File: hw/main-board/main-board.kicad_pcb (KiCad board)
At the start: 2 copper layers, 42 x 42 mm, 61 parts, among them J1 USB_C_Receptacle_USB2.0_16P, J2 S4B-XH-A_LF__SN_, J3 S4B-XH-A_LF__SN_, Q1 AONR21307, U1 HUSB238_xxxDD, U2 AP63205WU, U3 AP2112K-3.3, U4 PTR54L, U5 TMC2226-SA, U6 TMC2226-SA

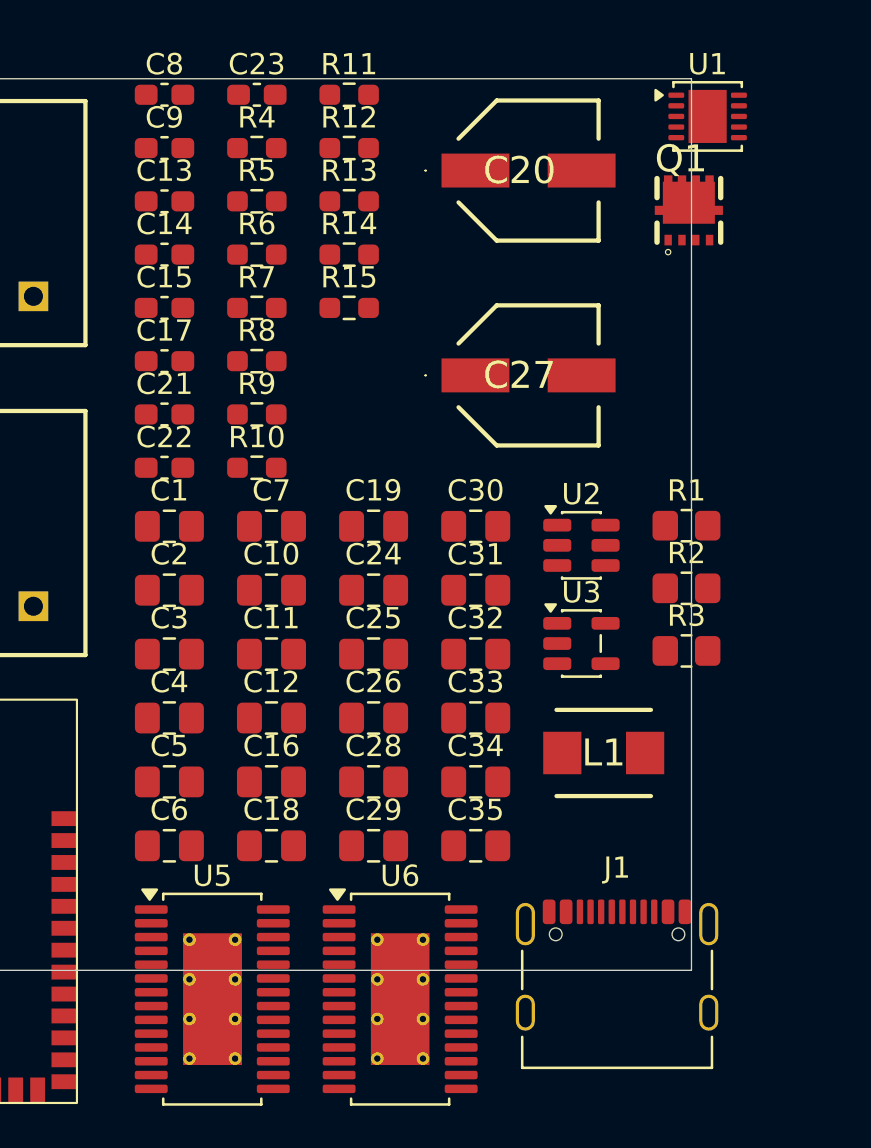
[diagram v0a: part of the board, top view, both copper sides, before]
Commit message: Add indicator LED
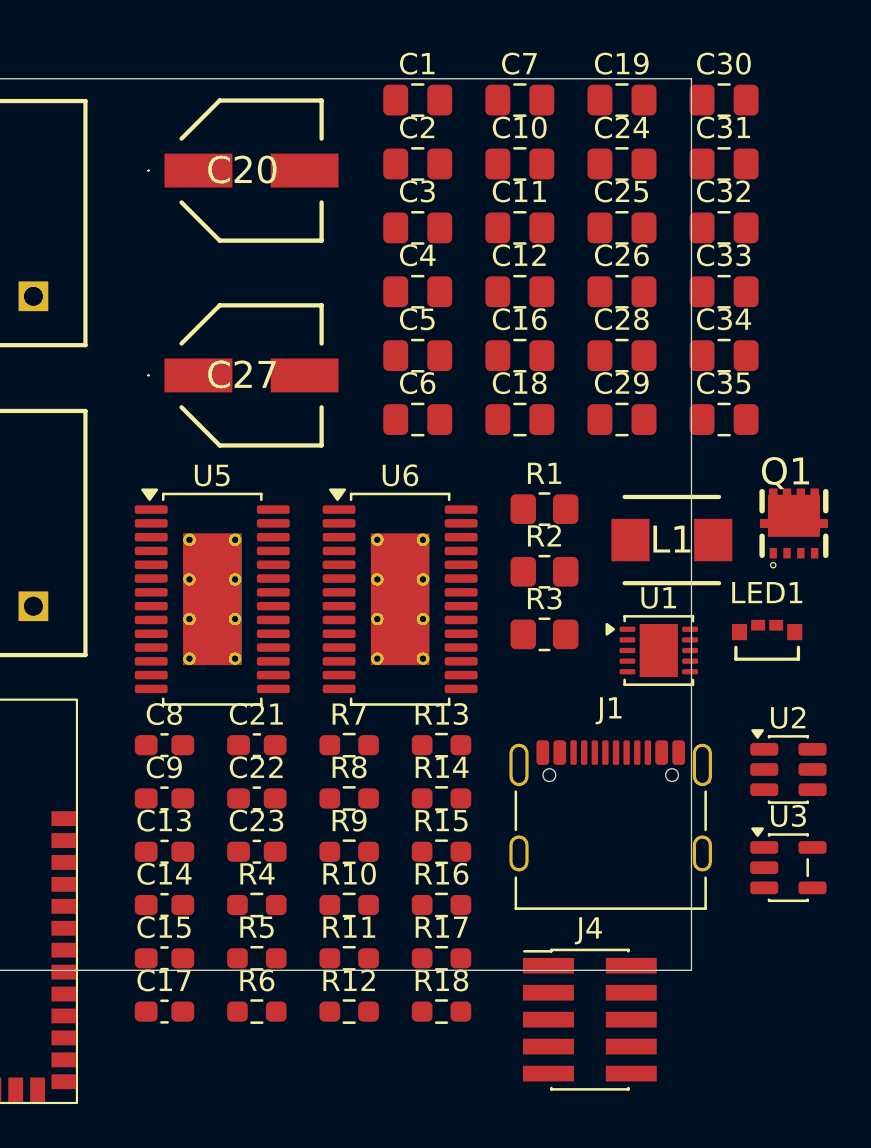
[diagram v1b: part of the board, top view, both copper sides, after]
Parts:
- added J4: Conn_ARM_JTAG_SWD_10, Connector_PinHeader_1.27mm:PinHeader_2x05_P1.27mm_Vertical_SMD, F.Cu at (161.7, 117.8)
- added LED1: 22-23C/R6GHBHW-C01/2C, Project_Specific_Parts:22-23C_EVE, F.Cu at (169.6, 99.2)
- added R16: 82R, Resistor_SMD:R_0603_1608Metric_Pad0.98x0.95mm_HandSolder, F.Cu at (154.7, 112.4)
- added R17: 82R, Resistor_SMD:R_0603_1608Metric_Pad0.98x0.95mm_HandSolder, F.Cu at (154.7, 114.9)
- added R18: 300R, Resistor_SMD:R_0603_1608Metric_Pad0.98x0.95mm_HandSolder, F.Cu at (154.7, 117.4)
- moved R11 40.7 mm to (150.4, 114.9)
- moved R12 40.7 mm to (150.4, 117.4)
- moved C23 35.7 mm to (146.0, 109.9)
- moved R4 35.7 mm to (146.0, 112.4)
- moved R5 35.7 mm to (146.0, 114.9)
- moved R6 35.7 mm to (146.0, 117.4)
- moved C13 30.6 mm to (141.7, 109.9)
- moved C14 30.6 mm to (141.7, 112.4)
- moved C15 30.6 mm to (141.7, 114.9)
- moved C8 30.6 mm to (141.7, 104.9)
- moved C9 30.6 mm to (141.7, 107.4)
- moved C17 30.6 mm to (141.7, 117.4)
- moved R14 26.0 mm to (154.7, 107.4)
- moved R15 26.0 mm to (154.7, 109.9)
- moved R13 26.0 mm to (154.7, 104.9)
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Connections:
- U4 pad 34: unconnected-(U4-RESET-Pad34) -> /RESET
- U4 pad 35: unconnected-(U4-SWDIO-Pad35) -> /SWDIO
- U4 pad 36: unconnected-(U4-SWCLK-Pad36) -> /SWCLK

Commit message: Add LED control IC (KTD2026)
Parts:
- moved LED1 11.4 mm to (158.6, 101.9)
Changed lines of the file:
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@@
 	(footprint "Project_Specific_Parts:22-23C_EVE"
 		(layer "F.Cu")
-		(at 169.6408 99.2442)
+		(at 158.575 101.890654)
 		(tags "22-23C/R6GHBHW-C01/2C ")
 		(property "Reference" "LED1"
@@
 		(sheetname "/")
 		(sheetfile "main-board.kicad_sch")
-		(units
-			(unit
-				(name "A")
-				(pins "4" "3" "2" "1")
-			)
-		)
 		(attr smd)
 		(duplicate_pad_numbers_are_jumpers no)
@@
 		(model "E:/Projects/Perde/hw/lib/SamacSys_Parts.3dshapes/22-23C_R6GHBHW-C01_2C.stp"
 			(offset
-				(xyz 0.4 -0.25 0.25)
+				(xyz 0.4 -0.15 0.25)
 			)
 			(scale

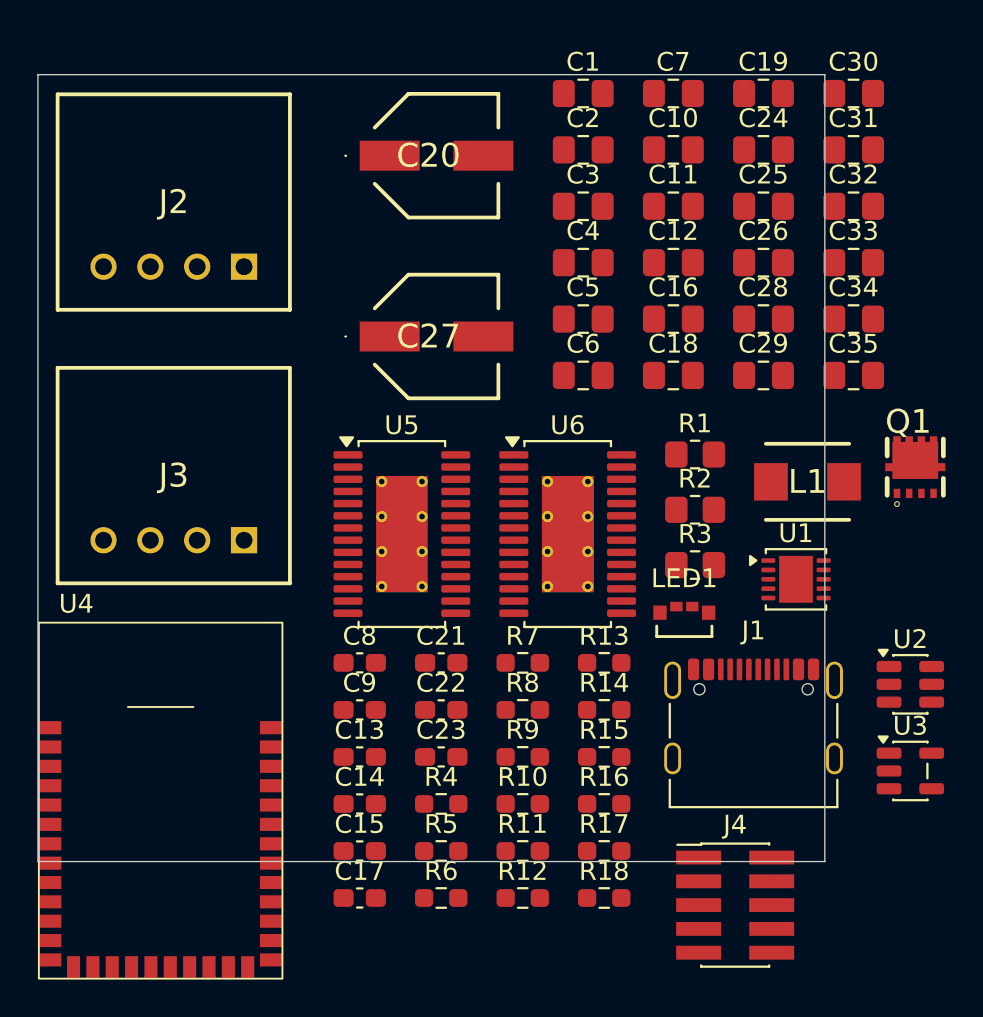
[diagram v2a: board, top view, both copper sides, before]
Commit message: Remove excessive cap for driver
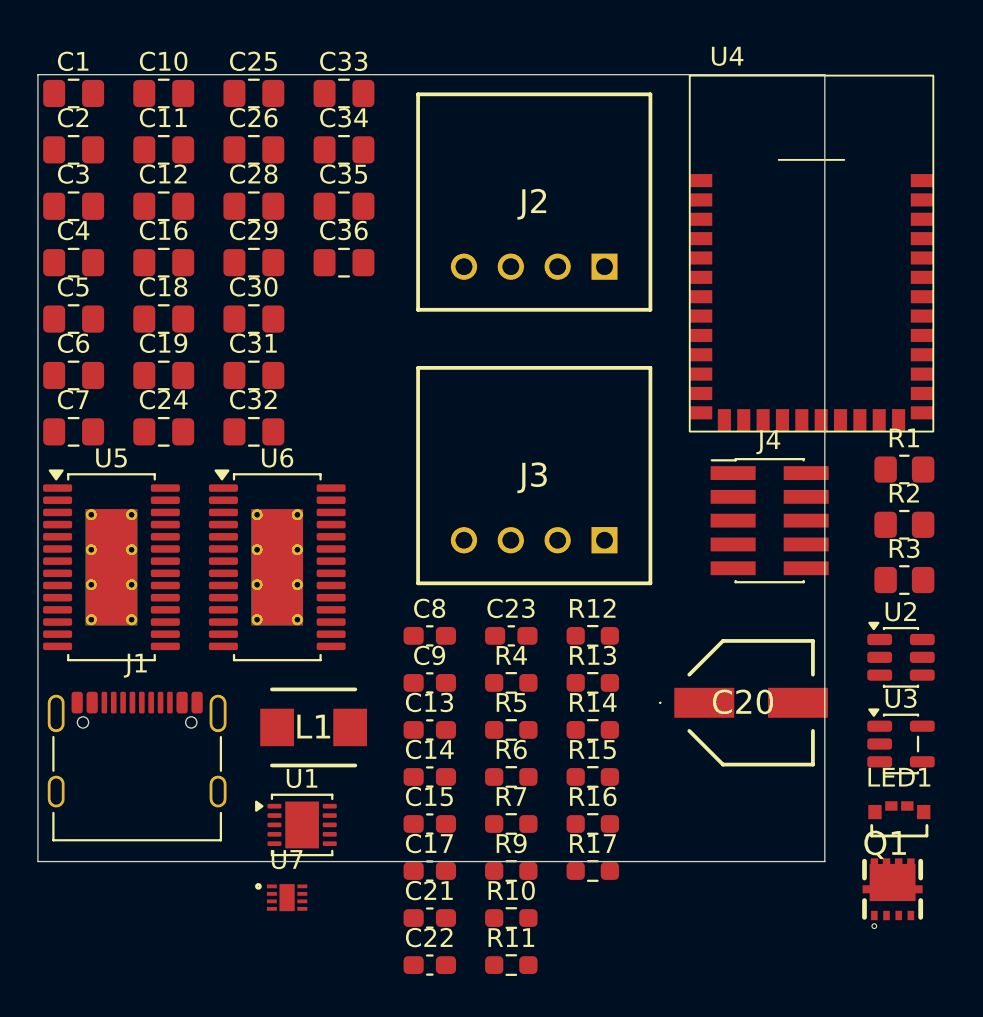
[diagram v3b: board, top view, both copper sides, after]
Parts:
- removed C27: EEE-FT1V101AP, Samacsys:EEE1AA101SP
- removed R18: 300R, Resistor_SMD:R_0603_1608Metric_Pad0.98x0.95mm_HandSolder
- removed R8: 1K, Resistor_SMD:R_0603_1608Metric_Pad0.98x0.95mm_HandSolder
- added C36: 4.7uF, Capacitor_SMD:C_0805_2012Metric_Pad1.18x1.45mm_HandSolder, F.Cu at (140.8, 83.5)
- added U7: KTD2026BEWE-TR, Project_Specific_Parts:UTDFN8_1P5X1P5_KIN, F.Cu at (137.8, 117.4)
- R16, R17: value 82R -> 2K2
- moved U4 45.4 mm to (165.8, 83.0)
- moved C7 36.8 mm to (126.4, 92.6)
- moved C19 35.4 mm to (131.2, 89.6)
- moved C24 35.4 mm to (131.2, 92.6)
- moved C30 34.2 mm to (136.0, 86.5)
- moved C31 34.2 mm to (136.0, 89.6)
- moved C32 34.2 mm to (136.0, 92.6)
- moved C20 33.7 mm to (162.6, 107.0)
- moved J1 32.9 mm to (129.8, 109.5)
- moved U1 29.4 mm to (138.6, 113.5)
- moved L1 29.4 mm to (139.2, 108.3)
- moved C33 28.7 mm to (140.8, 74.5)
- moved C34 28.7 mm to (140.8, 77.5)
- moved C35 28.7 mm to (140.8, 80.5)
- moved C25 27.9 mm to (136.0, 74.5)
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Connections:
- C16 pad 2: /VREF -> /VREF1
- C24 pad 2: /VREF -> /VREF2
- J4 pad 6: unconnected-(J4-SWO/TDO-Pad6) -> /SWO
- LED1 pad 2: Net-(LED1-Pad2) -> /GREEN
- LED1 pad 3: Net-(LED1-Pad3) -> /RED
- LED1 pad 4: Net-(LED1-Pad4) -> /BLUE
- R10 pad 1: /VREF -> /VREF1
- R11 pad 2: /UART_TX -> Net-(U4-P2.08)
- R14 pad 2: /EN1 -> /EN2
- R15 pad 1: /VREF -> /VREF2
- R16 pad 1: /GREEN -> /PD_SDA
- R16 pad 2: Net-(LED1-Pad2) -> +3.3V
- R17 pad 1: /BLUE -> /PD_SCL
- R17 pad 2: Net-(LED1-Pad4) -> +3.3V
- U4 pad 13: unconnected-(U4-P1.04-Pad13) -> /STEP1
- U4 pad 14: unconnected-(U4-P1.05-Pad14) -> /DIR1
- U4 pad 15: unconnected-(U4-P1.06-Pad15) -> /EN1
- U4 pad 16: unconnected-(U4-P1.07-Pad16) -> /STEP2
- U4 pad 17: unconnected-(U4-P1.08-Pad17) -> /DIAG2
- U4 pad 18: unconnected-(U4-P2.03-Pad18) -> /DIR2
- U4 pad 19: unconnected-(U4-P2.04-Pad19) -> /EN2
- U4 pad 23: unconnected-(U4-P2.02-Pad23) -> /SWO
- U4 pad 25: unconnected-(U4-P2.07-Pad25) -> /UART_RX
- U4 pad 26: unconnected-(U4-P2.08-Pad26) -> Net-(U4-P2.08)
- U4 pad 32: unconnected-(U4-P0.03-Pad32) -> /PD_SDA
- U4 pad 33: unconnected-(U4-P0.04-Pad33) -> /PD_SCL
- U4 pad 8: unconnected-(U4-P1.14-Pad8) -> /DIAG1
- U5 pad 11: /VREF -> /VREF1
- U6 pad 11: /VREF -> /VREF2
- U6 pad 15: /DIAG1 -> /DIAG2
- U6 pad 20: /STEP1 -> /STEP2
- U6 pad 23: /DIR1 -> /DIR2
- U6 pad 5: /EN1 -> /EN2

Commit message: Add not-connected labels
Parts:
- added S1: B3F-3100, Samacsys:B3F3100, F.Cu at (162.5, 110.0)
- moved U7 34.3 mm to (170.9, 108.6)
- moved LED1 32.7 mm to (137.7, 116.9)
- moved Q1 12.7 mm to (170.8, 104.3)
- moved C20 10.2 mm to (162.6, 117.3)
- moved U2 10.2 mm to (170.6, 114.8)
- moved U3 10.2 mm to (170.6, 119.5)
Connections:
- U4 pad 29: unconnected-(U4-P0.00-Pad29) -> /BUTTON

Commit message: Fix LED power source
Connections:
- C36 pad 1: +3.3V -> +5V
- LED1 pad 1: +3.3V -> +5V
- S1 pad 2: /BUTTON -> GND
- U7 pad 5: +3.3V -> +5V
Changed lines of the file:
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@@
 			(layers "*.Cu" "*.Mask")
 			(remove_unused_layers no)
-			(net "/BUTTON")
+			(net "GND")
 			(pinfunction "2_2")
 			(pintype "passive")
@@
 			(size 0.5334 0.2032)
 			(layers "F.Cu" "F.Mask" "F.Paste")
-			(net "+3.3V")
+			(net "+5V")
 			(pinfunction "VIN_5")
 			(pintype "power_in")
@@
 			(layers "F.Cu" "F.Mask" "F.Paste")
 			(roundrect_rratio 0.212766)
-			(net "+3.3V")
+			(net "+5V")
 			(pintype "passive")
 		)
@@
 			(size 0.7112 0.762)
 			(layers "F.Cu" "F.Mask" "F.Paste")
-			(net "+3.3V")
+			(net "+5V")
 			(pinfunction "1_1")
 			(pintype "power_in")
@@
 			(net "unconnected-(U4-P1.09-Pad3)")
 			(pinfunction "P1.09_3")
-			(pintype "bidirectional")
+			(pintype "bidirectional+no_connect")
 		)
 		(pad "4" smd rect
@@
 			(net "unconnected-(U4-P1.10-Pad4)")
 			(pinfunction "P1.10_4")
-			(pintype "bidirectional")
+			(pintype "bidirectional+no_connect")
 		)
 		(pad "5" smd rect
@@
 			(net "unconnected-(U4-P1.11-Pad5)")
 			(pinfunction "P1.11_5")
-			(pintype "bidirectional")
+			(pintype "bidirectional+no_connect")
 		)
 		(pad "6" smd rect
@@
 			(net "unconnected-(U4-P1.12-Pad6)")
 			(pinfunction "P1.12_6")
-			(pintype "bidirectional")
+			(pintype "bidirectional+no_connect")
 		)
 		(pad "7" smd rect
@@
 			(net "unconnected-(U4-P1.13-Pad7)")
 			(pinfunction "P1.13_7")
-			(pintype "bidirectional")
+			(pintype "bidirectional+no_connect")
 		)
 		(pad "8" smd rect
@@
 			(net "unconnected-(U4-P2.05-Pad20)")
 			(pinfunction "P2.05_20")
-			(pintype "bidirectional")
+			(pintype "bidirectional+no_connect")
 		)
 		(pad "21" smd rect
@@
 			(net "unconnected-(U4-P2.00-Pad21)")
 			(pinfunction "P2.00_21")
-			(pintype "bidirectional")
+			(pintype "bidirectional+no_connect")
 		)
 		(pad "22" smd rect
@@
 			(net "unconnected-(U4-P2.01-Pad22)")
 			(pinfunction "P2.01_22")
-			(pintype "bidirectional")
+			(pintype "bidirectional+no_connect")
 		)
 		(pad "23" smd rect
@@
 			(net "unconnected-(U4-P2.06-Pad24)")
 			(pinfunction "P2.06_24")
-			(pintype "bidirectional")
+			(pintype "bidirectional+no_connect")
 		)
 		(pad "25" smd rect
@@
 			(net "unconnected-(U4-P2.09-Pad27)")
 			(pinfunction "P2.09_27")
-			(pintype "bidirectional")
+			(pintype "bidirectional+no_connect")
 		)
 		(pad "28" smd rect
@@
 			(net "unconnected-(U4-P2.10-Pad28)")
 			(pinfunction "P2.10_28")
-			(pintype "bidirectional")
+			(pintype "bidirectional+no_connect")
 		)
 		(pad "29" smd rect
@@
 			(net "unconnected-(U4-P0.01-Pad30)")
 			(pinfunction "P0.01_30")
-			(pintype "bidirectional")
+			(pintype "bidirectional+no_connect")
 		)
 		(pad "31" smd rect
@@
 			(net "unconnected-(U4-P0.02-Pad31)")
 			(pinfunction "P0.02_31")
-			(pintype "bidirectional")
+			(pintype "bidirectional+no_connect")
 		)
 		(pad "32" smd rect

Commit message: Add rule area for TMC2226s
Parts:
- added D1: SMBJ16A, Samacsys:DIOM5436X261N, F.Cu at (179.6, 80.7)
- added D2: SS34, Diode_SMD:D_SMA, F.Cu at (179.6, 85.8)
- R4: value 10R -> 14K
- R5: value 10R -> 16K5
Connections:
- Q1 pad 5: VBUS -> Net-(D2-A)
- Q1 pad 6: VBUS -> Net-(D2-A)
- Q1 pad 7: VBUS -> Net-(D2-A)
- Q1 pad 8: VBUS -> Net-(D2-A)

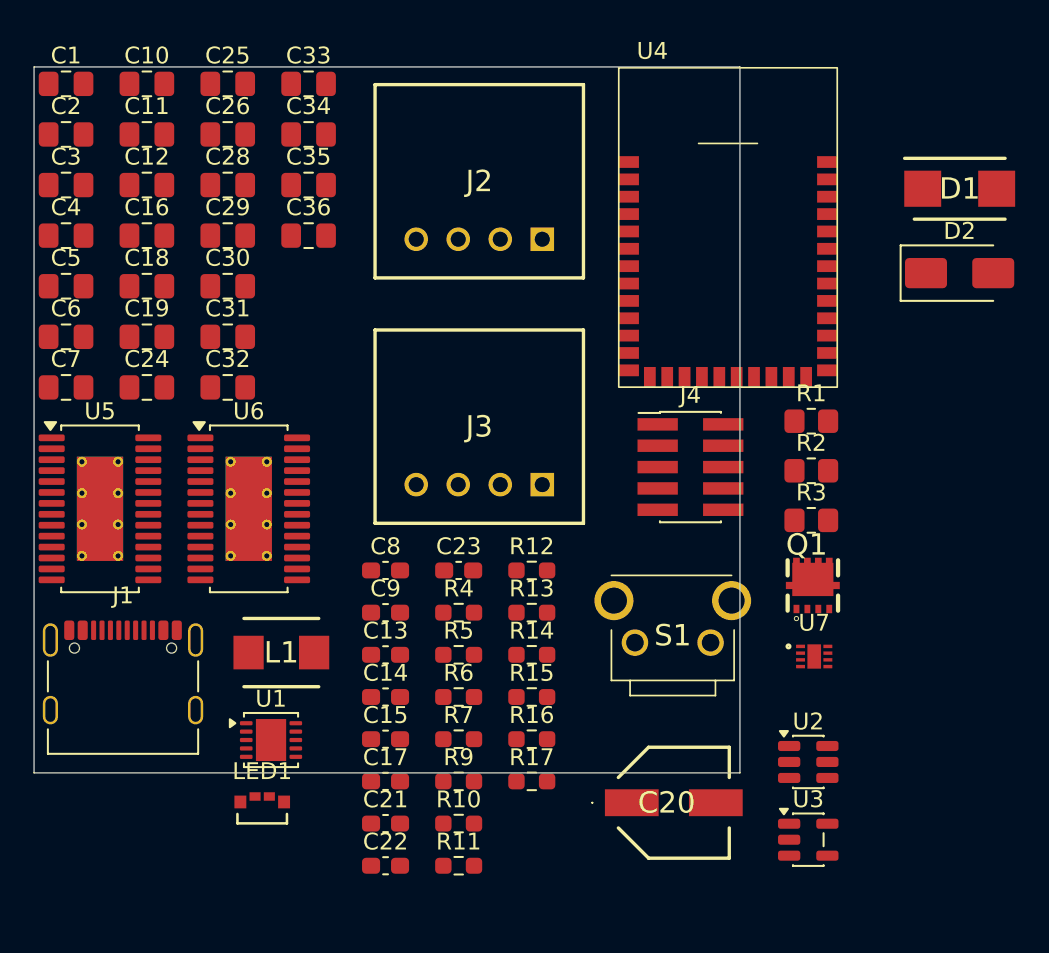
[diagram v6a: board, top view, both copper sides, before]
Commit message: Add component classes for TMC2226 circuit
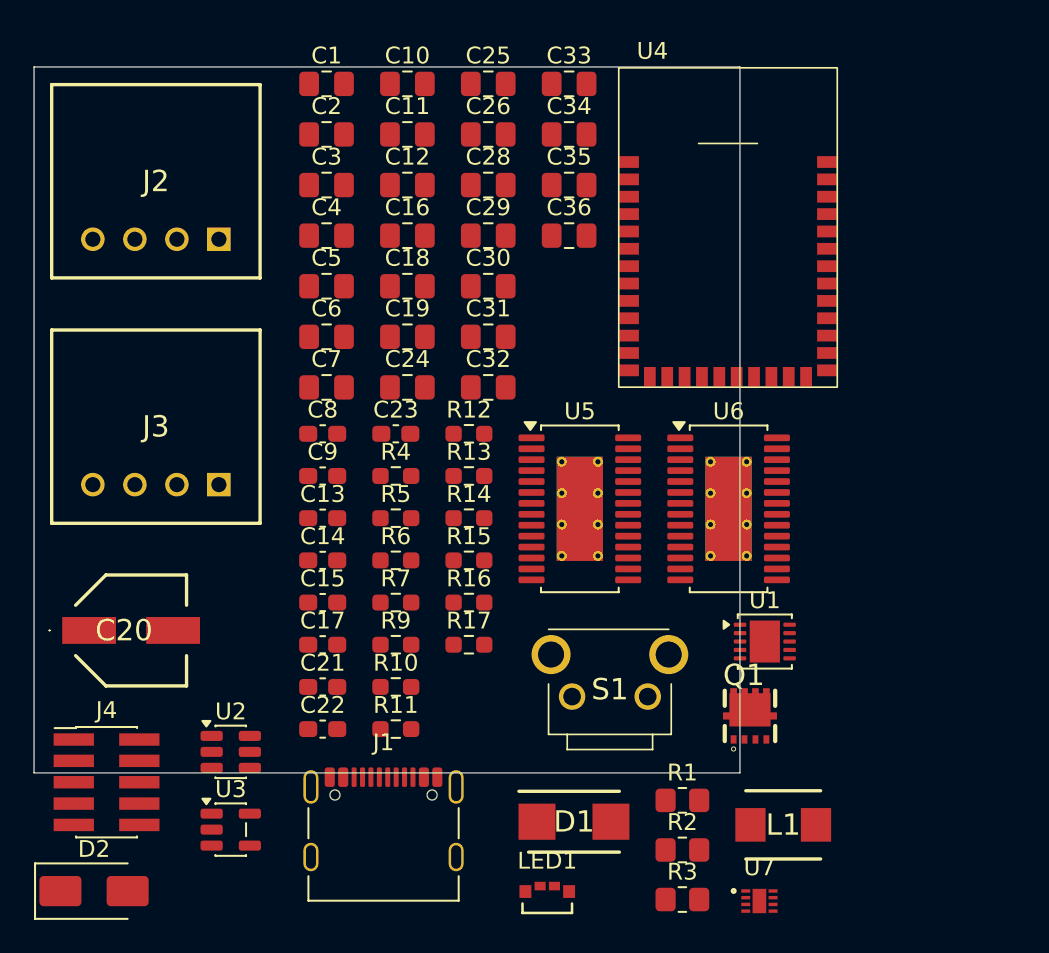
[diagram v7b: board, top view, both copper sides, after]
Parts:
- moved D2 63.3 mm to (128.1, 122.5)
- moved D1 44.1 mm to (156.6, 118.4)
- moved J4 39.5 mm to (128.8, 116.1)
- moved U2 34.4 mm to (136.2, 114.2)
- moved U3 34.4 mm to (136.2, 118.9)
- moved C20 33.9 mm to (130.3, 107.0)
- moved L1 31.6 mm to (169.1, 118.6)
- moved U1 30.0 mm to (168.0, 107.7)
- moved U5 28.5 mm to (157.0, 99.8)
- moved U6 28.5 mm to (165.8, 99.8)
- moved R1 23.8 mm to (163.1, 117.1)
- moved R3 23.8 mm to (163.1, 123.0)
- moved R2 23.8 mm to (163.1, 120.1)
- moved J2 19.2 mm to (135.5, 83.8)
- moved J3 19.2 mm to (135.5, 98.3)
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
